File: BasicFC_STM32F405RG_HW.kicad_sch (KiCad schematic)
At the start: 72 parts, among them J1 Conn_01x05, J2 Conn_02x02_Odd_Even, J3 Conn_02x02_Odd_Even, J4 USB_A, J6 Conn_01x08, U1 STM32F405RGTx, U2 TPS5430DDA, U3 RT9013-33GB, U4 MPU6000, U5 HMC5883L, U6 BMP280, U7 AT7456, Y1 8MHz, Y2 8MHz

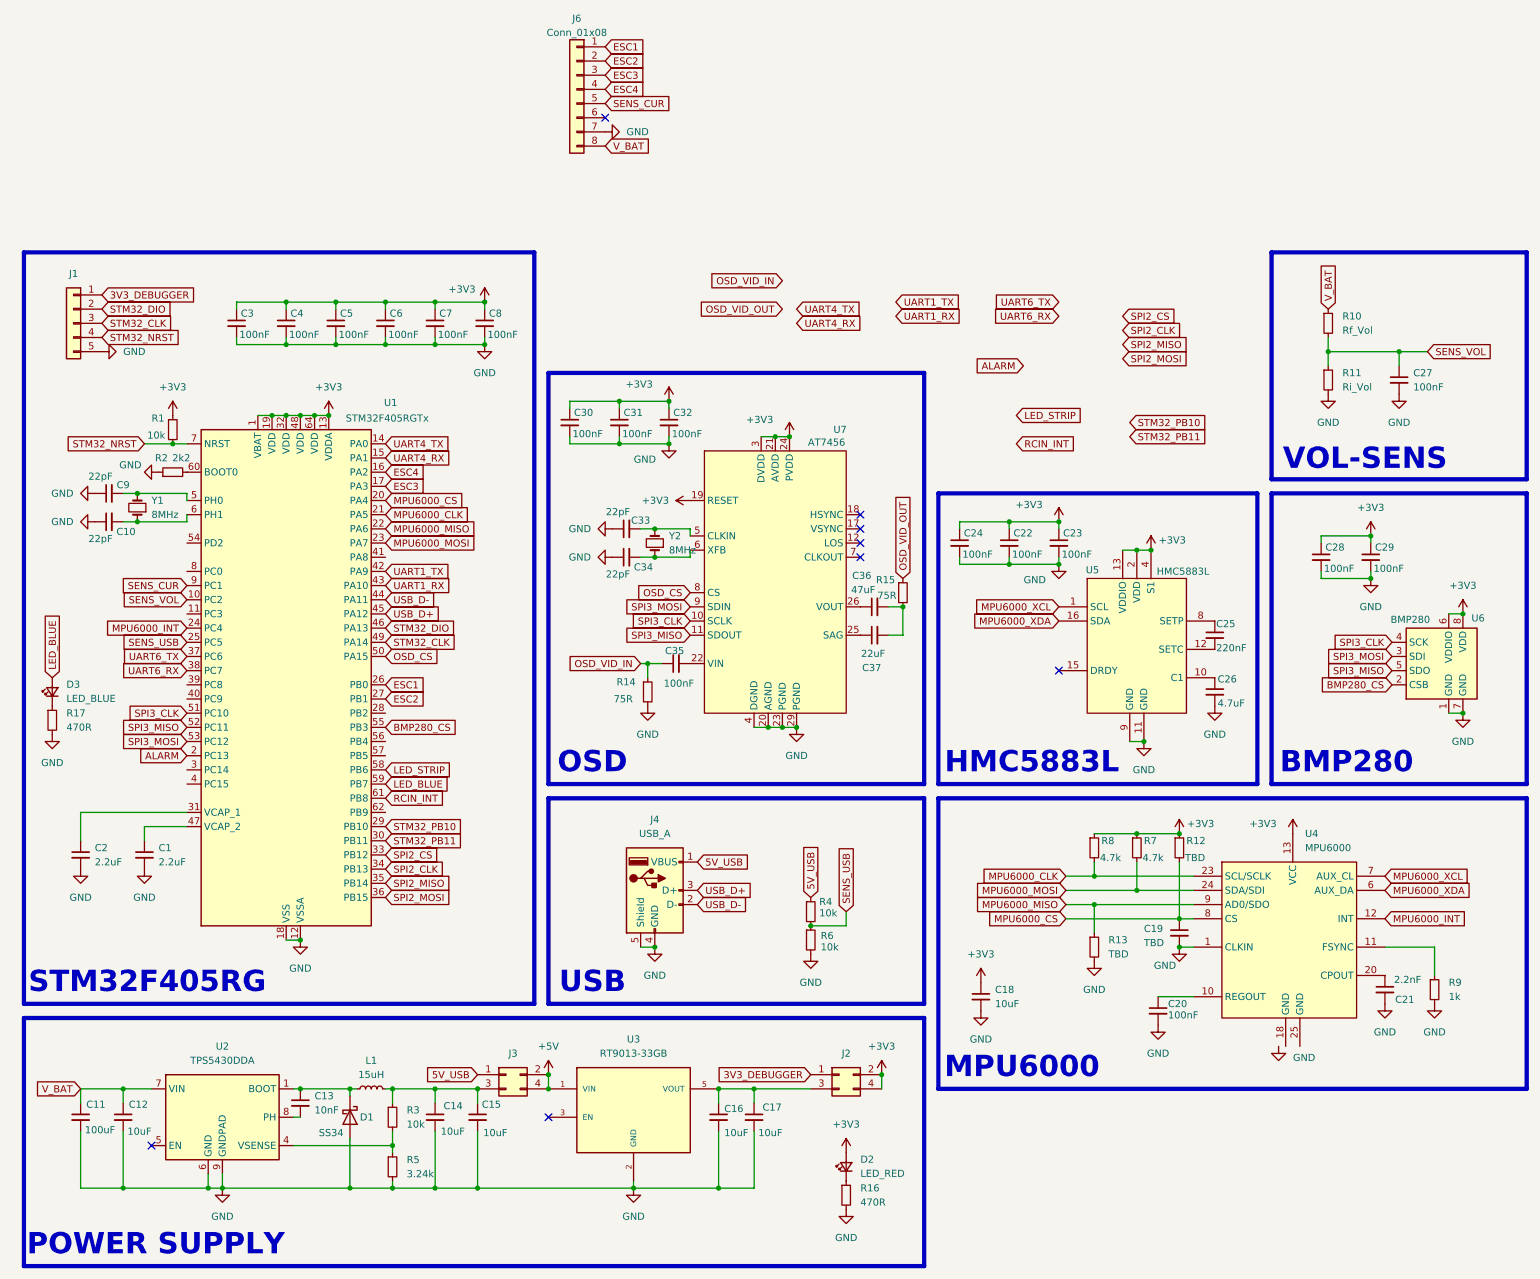
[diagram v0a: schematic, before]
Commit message: update schematic
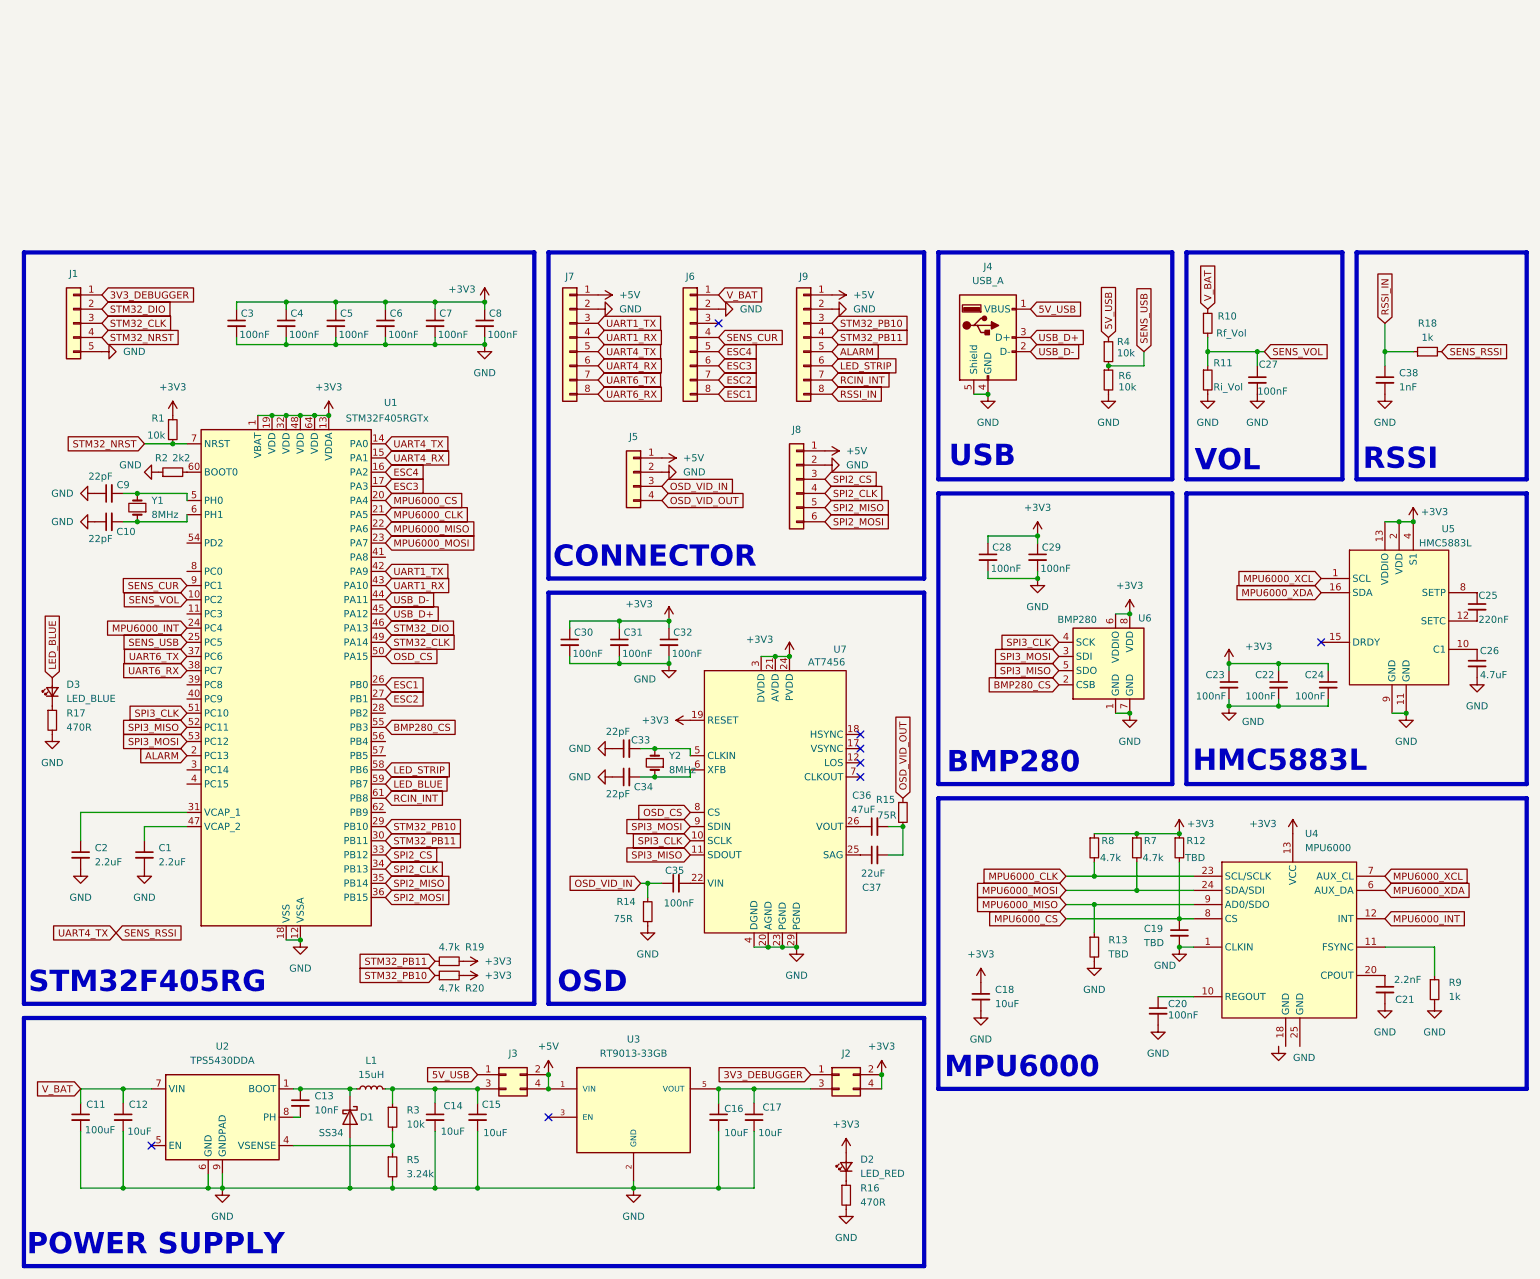
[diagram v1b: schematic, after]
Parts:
- added C38: 1nF, symbol Device:C_Small
- added J5: Conn_01x04, symbol Connector_Generic:Conn_01x04
- added J7, J9: Conn_01x08, symbol Connector_Generic:Conn_01x08
- added J8: Conn_01x06, symbol Connector_Generic:Conn_01x06
- added R18: 1k, symbol Device:R_Small
- added R19, R20: 4.7k, symbol Device:R_Small
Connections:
- net +3V3: now also R19.2, R20.2
- net +5V: now also J5.1 (Pin_1), J7.1 (Pin_1), J8.1 (Pin_1), J9.1 (Pin_1)
- net ALARM: now also J9.5 (Pin_5)
- net ESC1: now also J6.8 (Pin_8); no longer J6.1 (Pin_1)
- net ESC2: now also J6.7 (Pin_7); no longer J6.2 (Pin_2)
- net ESC3: now also J6.6 (Pin_6); no longer J6.3 (Pin_3)
- net ESC4: now also J6.5 (Pin_5); no longer J6.4 (Pin_4)
- net GND: now also J6.2 (Pin_2), C38.2, J5.2 (Pin_2), J7.2 (Pin_2), J8.2 (Pin_2), J9.2 (Pin_2); no longer J6.7 (Pin_7)
- net LED_STRIP: now also J9.6 (Pin_6)
- net OSD_VID_IN: now also J5.3 (Pin_3)
- net OSD_VID_OUT: now also J5.4 (Pin_4)
- net RCIN_INT: now also J9.7 (Pin_7)
- net SENS_CUR: now also J6.4 (Pin_4); no longer J6.5 (Pin_5)
- net SPI2_CLK: now also J8.4 (Pin_4)
- net SPI2_CS: now also J8.3 (Pin_3)
- net SPI2_MISO: now also J8.5 (Pin_5)
- net SPI2_MOSI: now also J8.6 (Pin_6)
- net STM32_PB10: now also J9.3 (Pin_3), R20.1
- net STM32_PB11: now also J9.4 (Pin_4), R19.1
- net UART1_RX: now also J7.4 (Pin_4)
- net UART1_TX: now also J7.3 (Pin_3)
- net UART4_RX: now also J7.6 (Pin_6)
- net UART6_RX: now also J7.8 (Pin_8)
- net UART6_TX: now also J7.7 (Pin_7)
- net V_BAT: now also J6.1 (Pin_1); no longer J6.8 (Pin_8)
- net UART4_TX renamed SENS_RSSI
- net SENS_RSSI: now also J7.5 (Pin_5), R18.2
- new net RSSI_IN: C38.1, J9.8 (Pin_8), R18.1
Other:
- note added: "CONNECTOR"
- note added: "RSSI"
- note added: "VOL"
- note removed: "VOL-SENS"
- moved on the sheet: C22, C23, C24, C25, C26, C27, C28, C29, C30, C31, C32, C33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
